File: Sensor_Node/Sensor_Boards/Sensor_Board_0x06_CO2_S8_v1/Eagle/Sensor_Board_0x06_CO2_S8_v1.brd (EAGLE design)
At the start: 55 x 35 mm, 16 parts, among them J1 M04_SMD_90, J2 5.5x2.1mm Barrel, J3 M03_SMD_90, J4 ARDUINO_ISP, U1 SENSEAIR_S8_SMD, U2 ATMEGA328P_TQFP, Y1 8MHZ

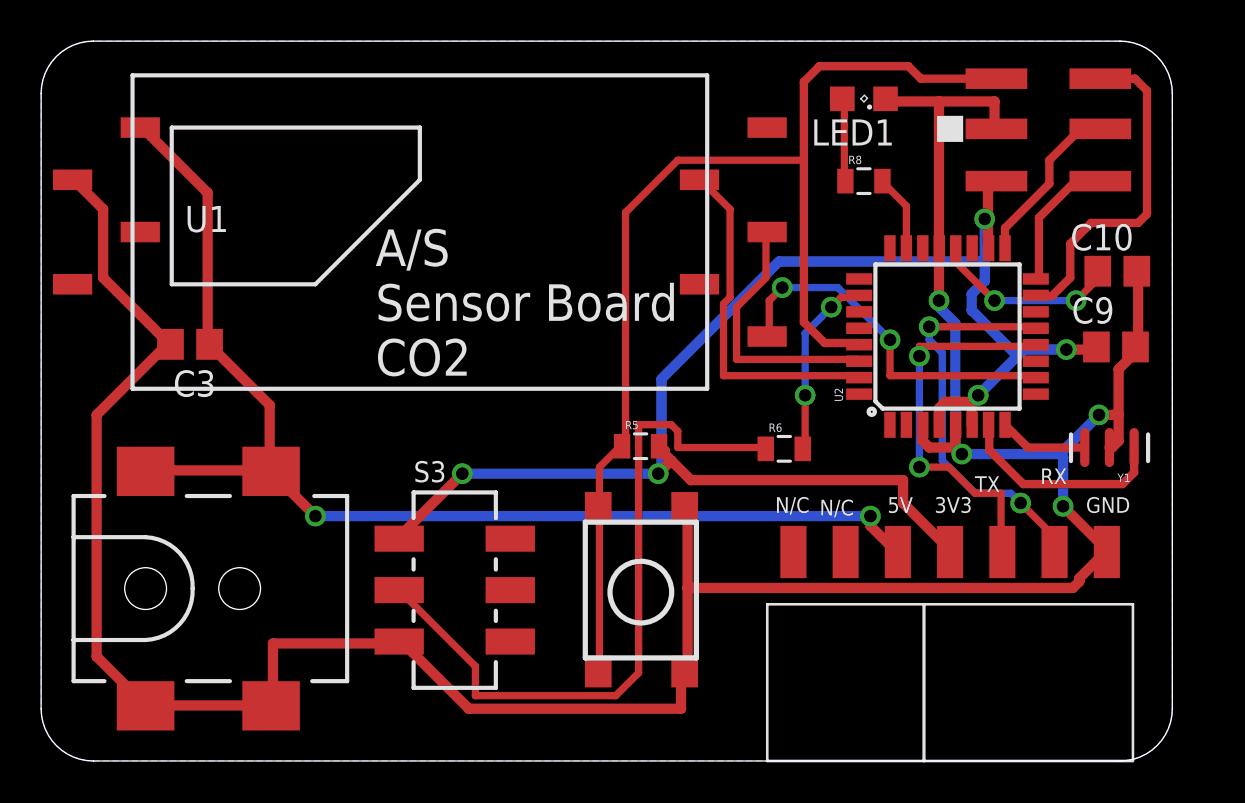
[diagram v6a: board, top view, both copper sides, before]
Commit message: Finished SHT31 and CO2-Board
- finished tidying SHT31
- added FTDI-connector to CO2-Sensorboard
- tidied CO2-Sensorboard
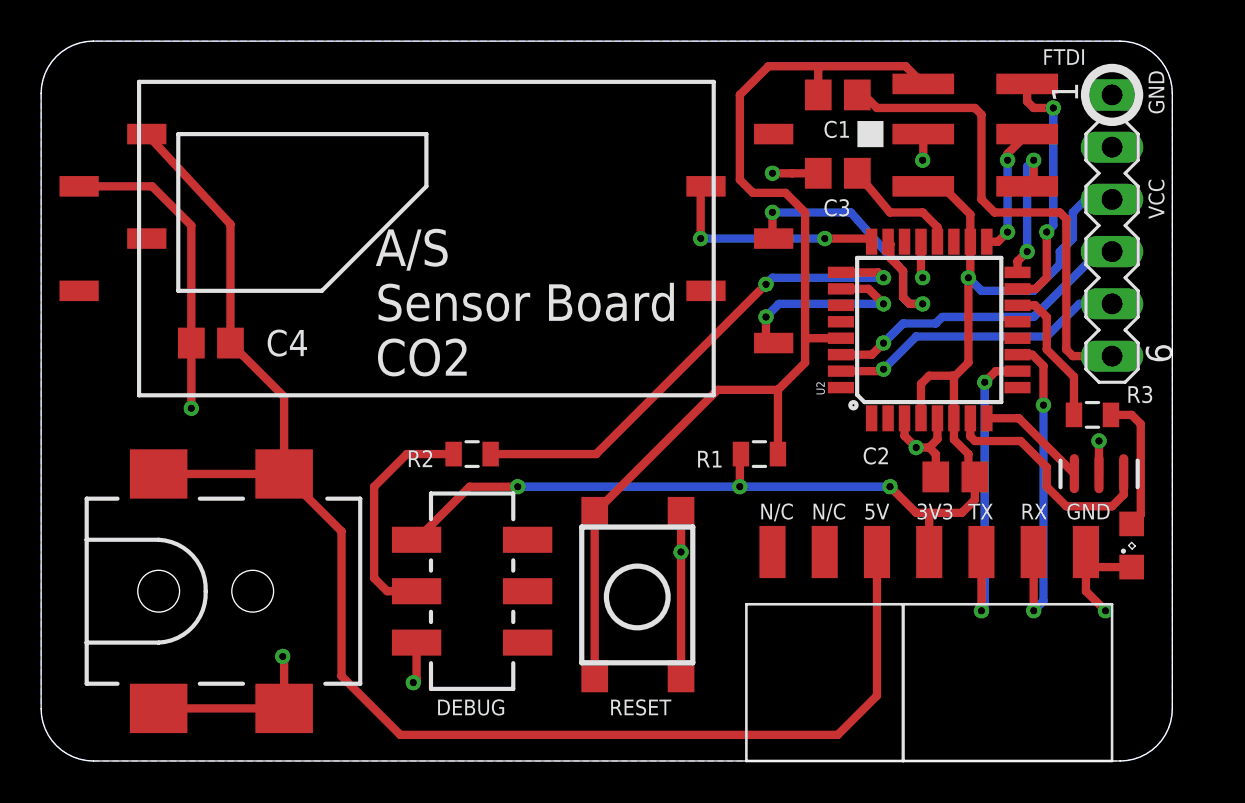
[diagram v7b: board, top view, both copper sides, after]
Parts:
- removed C10, C9: 100n, eagle-ltspice:C0805
- removed R5, R6: 10k, SparkFun-Passives:0805
- removed R8: 330, SparkFun-Passives:0805
- added C1, C2, C4: 100n, eagle-ltspice:C0805
- added R1, R2: 10k, SparkFun-Passives:0805
- added R3: 330, SparkFun-Passives:0805
- added SV1: (no value), con-lstb:MA06-1
- moved C3 32.6 mm to (38.7, 28.6)
- moved LED1 25.3 mm to (53.0, 10.5), turned to 90 degrees
- moved J4 3.57 mm to (47.9, 27.9)
- moved Y1 1.37 mm to (51.4, 14.0)
- moved J1 1.02 mm to (43.2, 10.2)
- moved J3 1.02 mm to (35.6, 10.2)
- moved U2 0.94 mm to (43.2, 21.0)
- moved S3 0.85 mm to (21.0, 8.26)
- moved J2 0.65 mm to (5.71, 8.26)
- moved U1 0.45 mm to (18.7, 25.4)
- moved S1 0.29 mm to (31.1, 12.1)
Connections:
- new net FTDI_RESET: C1.1, SV1.6
- new net FTDI_RXI: SV1.4, U2.30
- new net FTDI_TXO: SV1.5, U2.31
- net +3V3: now also C2.1, R1.2, SV1.3; no longer C9.1, R5.2
- net +5V: now also C4.1; no longer C3.1
- net DBG_ENABLE: now also R2.2, U2.25; no longer R6.2, U2.26
- net GND: now also C2.2, C4.2, SV1.1, SV1.2; no longer C10.2, C9.2
- net L1: now also R3.2, U2.14; no longer R8.2, U2.23
- net MCU_RXI: now also U2.11; no longer U2.13
- net MCU_TXO: now also U2.10; no longer U2.12
- net N$15: now also C3.1; no longer C10.1
- net N$30: now also R3.1; no longer R8.1
- net N$4: now also R2.1; no longer R6.1
- net RESET: now also C1.2, R1.1; no longer R5.1
- net SENS_CAL: now also U2.26; no longer U2.10
- net SENS_RX: now also U2.24; no longer U2.31
- net SENS_TX: now also U2.23; no longer U2.30
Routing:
- net GND: track 143.8 -> 51.6 mm, vias 4 -> 10
- net FTDI_RESET: track 0.00 -> 24.2 mm
- net N$4: track 34.2 -> 11.3 mm
- net DBG_ENABLE: track 9.08 -> 24.8 mm
- net FTDI_RXI: track 0.00 -> 15.3 mm, vias 0 -> 1
- net FTDI_TXO: track 0.00 -> 14.5 mm, vias 0 -> 1
- net +3V3: track 77.0 -> 63.7 mm, vias 5 -> 4
- net +5V: track 57.9 -> 71.3 mm, vias 2 -> 0
- net SENS_CAL: track 17.9 -> 9.94 mm
- net SENS_RX: track 16.9 -> 11.0 mm, vias 0 -> 2
- net RESET: track 57.4 -> 52.6 mm
- net MOSI: track 16.6 -> 12.3 mm, vias 0 -> 2
- net N$15: track 9.24 -> 5.79 mm, vias 2 -> 0
- net MCU_RXI: track 19.7 -> 16.5 mm
- net L1: track 3.74 -> 6.97 mm
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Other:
- board text added: "DEBUG"
- board text added: "FTDI"
- board text added: "RESET"
- board text added: "VCC"
